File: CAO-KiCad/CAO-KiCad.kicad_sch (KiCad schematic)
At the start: 8 parts, among them P1 Power, P2 Analog, P3 Digital, P4 Digital, P5 CONN_01X01, P6 CONN_01X01, P7 CONN_01X01, P8 CONN_01X01

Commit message: Debut de la creation du module ESP32
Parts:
- added D1: LED, LED_SMD:LED_0805_2012Metric_Pad1.15x1.40mm_HandSolder, symbol Device:LED
- added J1: Conn_01x03, Connector_PinHeader_2.54mm:PinHeader_1x03_P2.54mm_Vertical, symbol Connector_Generic:Conn_01x03
- added R1: 470, Resistor_SMD:R_0805_2012Metric_Pad1.20x1.40mm_HandSolder, symbol Device:R
- added U1: MODULE-38P-ESP32-WROOM-32D, RF_Module:ESP32-WROOM-32, symbol MCU_Module_Project:MODULE-38P-ESP32-WROOM-32D
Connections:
- net +5V: now also J1.2 (Pin_2), R1.1, U1.18 (SWP/SD3)
- net GND: now also D1.1 (K), J1.3 (Pin_3)
- new net: D1.2 (A), R1.2
- new net IO23: J1.1 (Pin_1)
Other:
- note added: "Configuration des cavaliers"
- note added: "Shield pour Arduino qui utilise la même disposition des broches comme la carte "Uno" Rev 3."
- note added: "TODO List: - ESP32-WROOM-32D - pont R pour LDR - Neopixel - MPU6050"
- note removed: "Shield for Arduino that uses the same pin disposition like "Uno" board Rev 3."
- company: Fab-Tronic -> ${COMPAGNY}
- title: Carte form factor Uno pour ESP32-WROOM-32D -> ${TITLE}

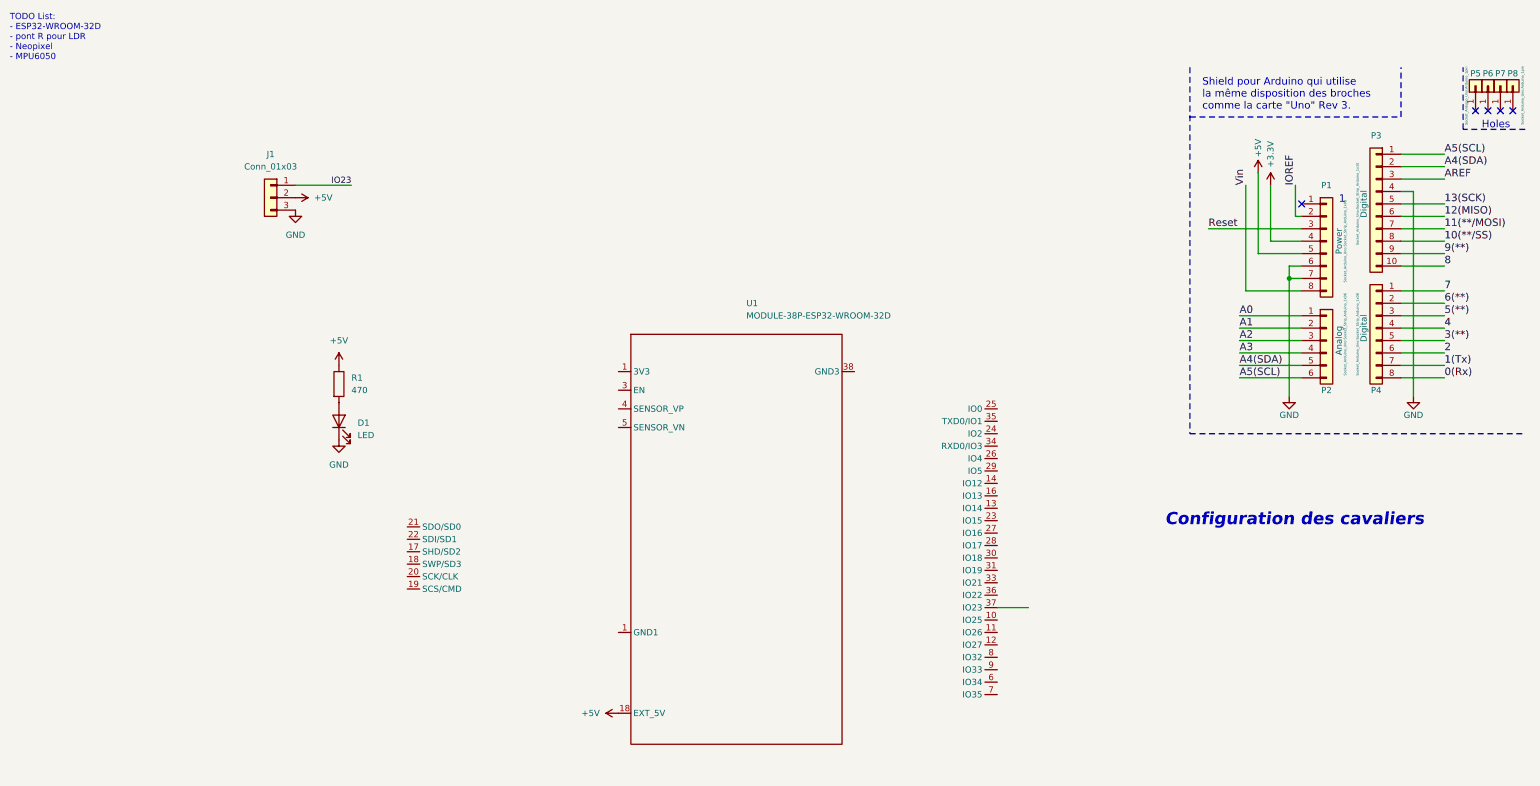
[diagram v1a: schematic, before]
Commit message: Arrangement des broches du symbole de l'ESP32
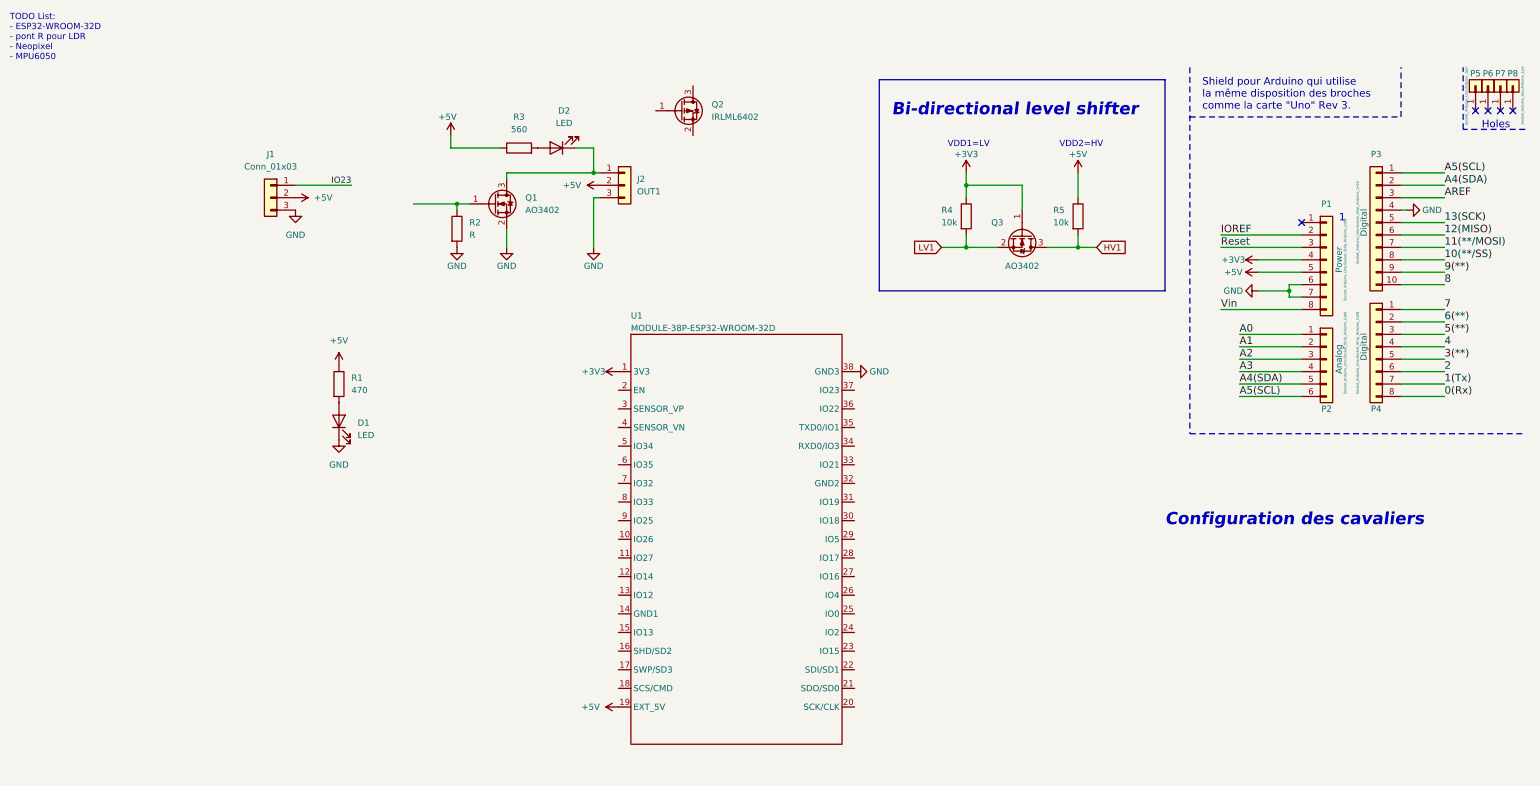
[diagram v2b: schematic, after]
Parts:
- added D2: LED, LED_SMD:LED_0805_2012Metric_Pad1.15x1.40mm_HandSolder, symbol Device:LED
- added J2: OUT1, Connector_PinHeader_2.54mm:PinHeader_1x03_P2.54mm_Vertical, symbol Connector_Generic:Conn_01x03
- added Q1, Q3: AO3402, Package_TO_SOT_SMD:SOT-23, symbol Transistor_FET:AO3400A
- added Q2: IRLML6402, Package_TO_SOT_SMD:SOT-23, symbol Transistor_FET:AO3401A
- added R2: R, Resistor_SMD:R_0805_2012Metric_Pad1.20x1.40mm_HandSolder, symbol Device:R
- added R3: 560, Resistor_SMD:R_0805_2012Metric_Pad1.20x1.40mm_HandSolder, symbol Device:R
- added R4, R5: 10k, Resistor_SMD:R_0805_2012Metric_Pad1.20x1.40mm_HandSolder, symbol Device:R
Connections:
- net +3V3: now also U1.1 (3V3), Q3.1 (G), R4.1
- net +5V: now also U1.19 (EXT_5V), J2.2 (Pin_2), R3.1, R5.1; no longer U1.18 (SWP/SD3)
- net GND: now also U1.38 (GND3), J2.3 (Pin_3), Q1.2 (S), R2.2
- new net: D2.2 (A), R3.2
- new net: D2.1 (K), J2.1 (Pin_1), Q1.3 (D)
- new net: Q1.1 (G), R2.1
- new net HV1: Q3.3 (D), R5.2
- new net LV1: Q3.2 (S), R4.2
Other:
- note added: "Bi-directional level shifter"
- note added: "VDD1=LV"
- note added: "VDD2=HV"
- moved on the sheet: P1, P2, P3, P4

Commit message: MAJ empreinte
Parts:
- added S1: Gaz_Sensor, Package_TO_SOT_THT:TO-5-2_Window, symbol My_sensor:Gaz_Sensor
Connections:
- net +5V: now also S1.2
- net GND: now also S1.3
- net at U1.4 (SENSOR_VN): now also S1.1 (Heater)
- net at U1.9 (IO25): now also S1.4
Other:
- moved on the sheet: U1
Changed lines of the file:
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@@
     (stroke (width 0) (type default) (color 0 0 0 0))
   )
+  (wire (pts (xy 90.17 119.38) (xy 90.17 127))
+    (stroke (width 0) (type default) (color 0 0 0 0))
+  )
   (polyline (pts (xy 152.4 15.24) (xy 152.4 58.42))
     (stroke (width 0) (type default) (color 0 0 0 0))
@@
     (stroke (width 0) (type solid) (color 0 0 0 0))
   )
+  (wire (pts (xy 96.52 114.3) (xy 96.52 111.76))
+    (stroke (width 0) (type default) (color 0 0 0 0))
+  )
   (wire (pts (xy 193.04 46.99) (xy 193.04 49.53))
     (stroke (width 0) (type default) (color 0 0 0 0))
@@
     (stroke (width 0) (type default) (color 0 0 0 0))
   )
+  (wire (pts (xy 90.17 114.3) (xy 96.52 114.3))
+    (stroke (width 0) (type default) (color 0 0 0 0))
+  )
   (wire (pts (xy 259.08 57.15) (xy 267.97 57.15))
     (stroke (width 0) (type solid) (color 0 0 0 0))
@@
     (stroke (width 0) (type solid) (color 0 0 0 0))
   )
+  (wire (pts (xy 64.77 92.71) (xy 64.77 109.22))
+    (stroke (width 0) (type default) (color 0 0 0 0))
+  )
+  (wire (pts (xy 64.77 119.38) (xy 72.39 119.38))
+    (stroke (width 0) (type default) (color 0 0 0 0))
+  )
   (wire (pts (xy 259.08 34.29) (xy 267.97 34.29))
     (stroke (width 0) (type solid) (color 0 0 0 0))
@@
     (stroke (width 0) (type solid) (color 0 0 0 0))
   )
+  (wire (pts (xy 106.68 92.71) (xy 64.77 92.71))
+    (stroke (width 0) (type default) (color 0 0 0 0))
+  )
   (wire (pts (xy 93.98 39.37) (xy 93.98 49.53))
     (stroke (width 0) (type default) (color 0 0 0 0))
@@
     (stroke (width 0) (type default) (color 0 0 0 0))
   )
+  (wire (pts (xy 64.77 109.22) (xy 72.39 109.22))
+    (stroke (width 0) (type default) (color 0 0 0 0))
+  )
   (wire (pts (xy 259.08 80.01) (xy 267.97 80.01))
     (stroke (width 0) (type solid) (color 0 0 0 0))
@@
     (stroke (width 0) (type solid) (color 0 0 0 0))
   )
+  (wire (pts (xy 96.52 111.76) (xy 106.68 111.76))
+    (stroke (width 0) (type default) (color 0 0 0 0))
+  )
   (polyline (pts (xy 215.9 22.86) (xy 259.08 22.86))
     (stroke (width 0) (type dash) (color 0 0 0 0))
   )
-  (image (at 123.19 109.22) (scale 0.672226)
+  (image (at 130.81 115.57) (scale 0.672226)
     (data
       iVBORw0KGgoAAAANSUhEUgAAAuAAAAWXCAYAAAAGXsH+AAAABHNCSVQICAgIfAhkiAAAAAlwSFlz
@@
     (pin "2")
   )
-  (symbol (lib_id "power:GND") (at 147.32 74.93 90) (unit 1)
+  (symbol (lib_id "power:GND") (at 154.94 81.28 90) (unit 1)
     (in_bom yes) (on_board yes)
-    (property "Reference" "#PWR018" (id 0) (at 153.67 74.93 0)
+    (property "Reference" "#PWR018" (id 0) (at 161.29 81.28 0)
       (effects (font (size 1.27 1.27)) hide)
     )
-    (property "Value" "GND" (id 1) (at 152.4 74.93 90))
-    (property "Footprint" "" (id 2) (at 147.32 74.93 0)
+    (property "Value" "GND" (id 1) (at 160.02 81.28 90))
+    (property "Footprint" "" (id 2) (at 154.94 81.28 0)
       (effects (font (size 1.27 1.27)) hide)
     )
-    (property "Datasheet" "" (id 3) (at 147.32 74.93 0)
+    (property "Datasheet" "" (id 3) (at 154.94 81.28 0)
+      (effects (font (size 1.27 1.27)) hide)
+    )
+    (pin "1")
+  )
+  (symbol (lib_id "power:GND") (at 90.17 127 0) (unit 1)
+    (in_bom yes) (on_board yes) (fields_autoplaced)
+    (property "Reference" "#PWR0101" (id 0) (at 90.17 133.35 0)
+      (effects (font (size 1.27 1.27)) hide)
+    )
+    (property "Value" "GND" (id 1) (at 90.17 132.08 0))
+    (property "Footprint" "" (id 2) (at 90.17 127 0)
+      (effects (font (size 1.27 1.27)) hide)
+    )
+    (property "Datasheet" "" (id 3) (at 90.17 127 0)
       (effects (font (size 1.27 1.27)) hide)
     )
@@
       (effects (font (size 1.27 1.27) italic) (justify left) hide)
     )
-    (property "Datasheet" "http://aosmd.com/pdfs/datasheet/AO3402.pdf" (id 3) (at 181.61 46.99 0)
+    (property "Datasheet" "http://www.aosmd.com/pdfs/datasheet/AO3400A.pdf" (id 3) (at 181.61 46.99 0)
       (effects (font (size 1.27 1.27)) (justify left) hide)
     )
@@
     (pin "1")
   )
-  (symbol (lib_id "MCU_Module_Project:MODULE-38P-ESP32-WROOM-32D") (at 123.19 107.95 0) (unit 1)
+  (symbol (lib_id "MCU_Module_Project:MODULE-38P-ESP32-WROOM-32D") (at 130.81 114.3 0) (unit 1)
     (in_bom yes) (on_board yes)
-    (property "Reference" "U1" (id 0) (at 101.6 63.5 0)
+    (property "Reference" "U1" (id 0) (at 109.22 69.85 0)
       (effects (font (size 1.27 1.27)) (justify left))
     )
-    (property "Value" "MODULE-38P-ESP32-WROOM-32D" (id 1) (at 101.6 66.04 0)
+    (property "Value" "MODULE-38P-ESP32-WROOM-32D" (id 1) (at 109.22 72.39 0)
       (effects (font (size 1.27 1.27)) (justify left))
     )
-    (property "Footprint" "RF_Module:ESP32-WROOM-32" (id 2) (at 123.19 156.21 0)
+    (property "Footprint" "RF_Module:ESP32-WROOM-32" (id 2) (at 130.81 162.56 0)
       (effects (font (size 1.27 1.27)) hide)
     )
-    (property "Datasheet" "https://www.espressif.com/sites/default/files/documentation/esp32-wroom-32d_esp32-wroom-32u_datasheet_en.pdf" (id 3) (at 123.19 162.56 0)
+    (property "Datasheet" "https://www.espressif.com/sites/default/files/documentation/esp32-wroom-32d_esp32-wroom-32u_datasheet_en.pdf" (id 3) (at 130.81 168.91 0)
       (effects (font (size 1.27 1.27)) hide)
     )
@@
     (pin "1")
   )
+  (symbol (lib_id "My_sensor:Gaz_Sensor") (at 81.28 114.3 0) (unit 1)
+    (in_bom yes) (on_board yes) (fields_autoplaced)
+    (property "Reference" "S1" (id 0) (at 81.28 102.87 0))
+    (property "Value" "Gaz_Sensor" (id 1) (at 81.28 105.41 0))
+    (property "Footprint" "Package_TO_SOT_THT:TO-5-2_Window" (id 2) (at 81.28 114.3 0)
+      (effects (font (size 1.27 1.27)) hide)
+    )
+    (property "Datasheet" "" (id 3) (at 81.28 114.3 0)
+      (effects (font (size 1.27 1.27)) hide)
+    )
+    (pin "1")
+    (pin "2")
+    (pin "3")
+    (pin "4")
+  )
   (symbol (lib_id "Device:LED") (at 86.36 29.21 180) (unit 1)
     (in_bom yes) (on_board yes) (fields_autoplaced)
@@
       (effects (font (size 1.27 1.27) italic) (justify left) hide)
     )
-    (property "Datasheet" "http://aosmd.com/pdfs/datasheet/AO3402.pdf" (id 3) (at 73.66 40.64 0)
+    (property "Datasheet" "http://www.aosmd.com/pdfs/datasheet/AO3400A.pdf" (id 3) (at 73.66 40.64 0)
       (effects (font (size 1.27 1.27)) (justify left) hide)
     )
@@
     (pin "3")
   )
-  (symbol (lib_id "power:+5V") (at 99.06 143.51 90) (unit 1)
+  (symbol (lib_id "power:+5V") (at 106.68 149.86 90) (unit 1)
     (in_bom yes) (on_board yes) (fields_autoplaced)
-    (property "Reference" "#PWR07" (id 0) (at 102.87 143.51 0)
+    (property "Reference" "#PWR07" (id 0) (at 110.49 149.86 0)
       (effects (font (size 1.27 1.27)) hide)
     )
-    (property "Value" "+5V" (id 1) (at 95.25 143.5099 90)
+    (property "Value" "+5V" (id 1) (at 102.87 149.8599 90)
       (effects (font (size 1.27 1.27)) (justify left))
     )
-    (property "Footprint" "" (id 2) (at 99.06 143.51 0)
+    (property "Footprint" "" (id 2) (at 106.68 149.86 0)
       (effects (font (size 1.27 1.27)) hide)
     )
-    (property "Datasheet" "" (id 3) (at 99.06 143.51 0)
+    (property "Datasheet" "" (id 3) (at 106.68 149.86 0)
       (effects (font (size 1.27 1.27)) hide)
     )
@@
       (effects (font (size 1.27 1.27) italic) (justify left) hide)
     )
-    (property "Datasheet" "https://www.infineon.com/dgdl/Infineon-IRLML6402-DataSheet-v01_01-EN.pdf?fileId=5546d462533600a401535668d5c2263c" (id 3) (at 111.76 21.59 0)
+    (property "Datasheet" "http://www.aosmd.com/pdfs/datasheet/AO3401A.pdf" (id 3) (at 111.76 21.59 0)
       (effects (font (size 1.27 1.27)) (justify left) hide)
     )
@@
     (pin "2")
   )
-  (symbol (lib_id "power:+3V3") (at 99.06 74.93 90) (unit 1)
+  (symbol (lib_id "power:+3V3") (at 106.68 81.28 90) (unit 1)
     (in_bom yes) (on_board yes)
-    (property "Reference" "#PWR017" (id 0) (at 102.87 74.93 0)
+    (property "Reference" "#PWR017" (id 0) (at 110.49 81.28 0)
       (effects (font (size 1.27 1.27)) hide)
     )
-    (property "Value" "+3V3" (id 1) (at 93.98 74.93 90))
-    (property "Footprint" "" (id 2) (at 99.06 74.93 0)
+    (property "Value" "+3V3" (id 1) (at 101.6 81.28 90))
+    (property "Footprint" "" (id 2) (at 106.68 81.28 0)
       (effects (font (size 1.27 1.27)) hide)
     )
-    (property "Datasheet" "" (id 3) (at 99.06 74.93 0)
+    (property "Datasheet" "" (id 3) (at 106.68 81.28 0)
       (effects (font (size 1.27 1.27)) hide)
     )
@@
     (pin "1")
   )
+  (symbol (lib_id "power:+5V") (at 64.77 119.38 0) (unit 1)
+    (in_bom yes) (on_board yes) (fields_autoplaced)
+    (property "Reference" "#PWR0102" (id 0) (at 64.77 123.19 0)
+      (effects (font (size 1.27 1.27)) hide)
+    )
+    (property "Value" "+5V" (id 1) (at 64.77 114.3 0))
+    (property "Footprint" "" (id 2) (at 64.77 119.38 0)
+      (effects (font (size 1.27 1.27)) hide)
+    )
+    (property "Datasheet" "" (id 3) (at 64.77 119.38 0)
+      (effects (font (size 1.27 1.27)) hide)
+    )
+    (pin "1")
+  )
   (symbol (lib_id "Connector_Generic:Conn_01x03") (at 100.33 36.83 0) (unit 1)
     (in_bom yes) (on_board yes) (fields_autoplaced)
@@
       (reference "#PWR018") (unit 1) (value "GND") (footprint "")
     )
+    (path "/05e71ddc-f3a7-42d8-be00-899197944b0d"
+      (reference "#PWR0101") (unit 1) (value "GND") (footprint "")
+    )
+    (path "/d84121f8-3010-4078-adb8-4eec39b429df"
+      (reference "#PWR0102") (unit 1) (value "+5V") (footprint "")
+    )
     (path "/f503ea07-bcf1-4924-930a-6f7e9cd312f8"
       (reference "D1") (unit 1) (value "LED") (footprint "LED_SMD:LED_0805_2012Metric_Pad1.15x1.40mm_HandSolder")
@@
       (reference "R5") (unit 1) (value "10k") (footprint "Resistor_SMD:R_0805_2012Metric_Pad1.20x1.40mm_HandSolder")
     )
+    (path "/8c40f36e-c660-4e3f-bacf-945ccf8cff0b"
+      (reference "S1") (unit 1) (value "Gaz_Sensor") (footprint "Package_TO_SOT_THT:TO-5-2_Window")
+    )
     (path "/5ab2e52c-e1f8-4d9a-8800-afae2c63ae8e"
